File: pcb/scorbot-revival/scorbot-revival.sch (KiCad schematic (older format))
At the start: 4 parts, among them J1 DB-50, J2 Raspberry_Pi_2_3, U1 L293D, U2 PIC18F2431-E_SP

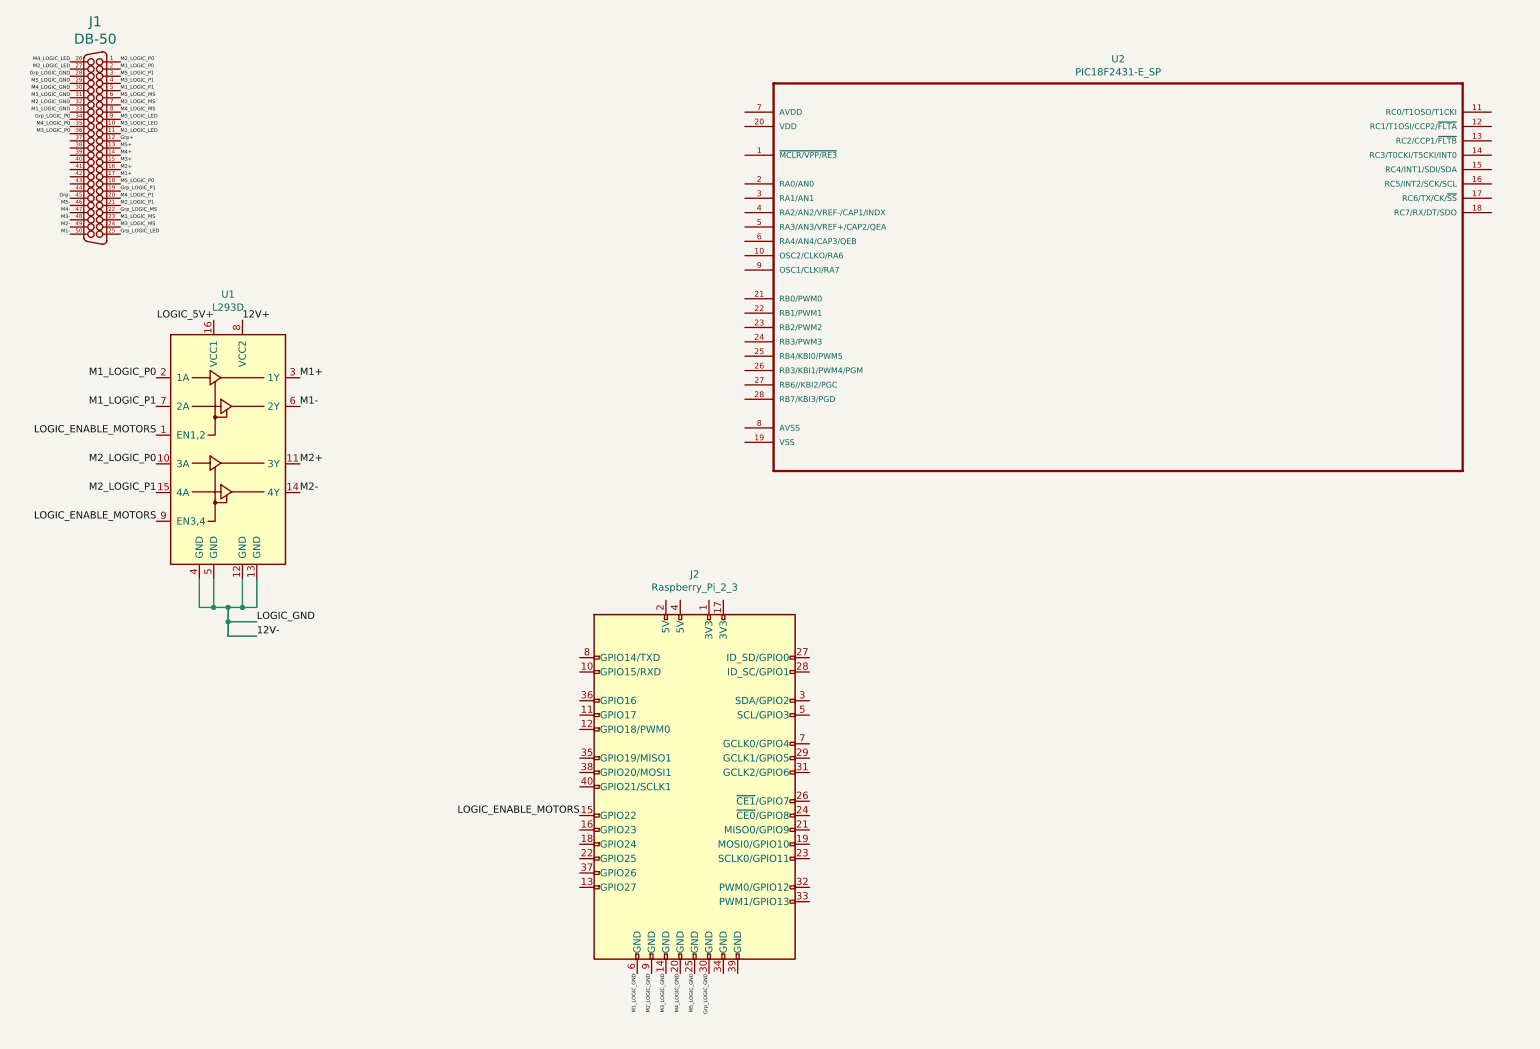
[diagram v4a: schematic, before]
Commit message: [pcb] pcbnew updates
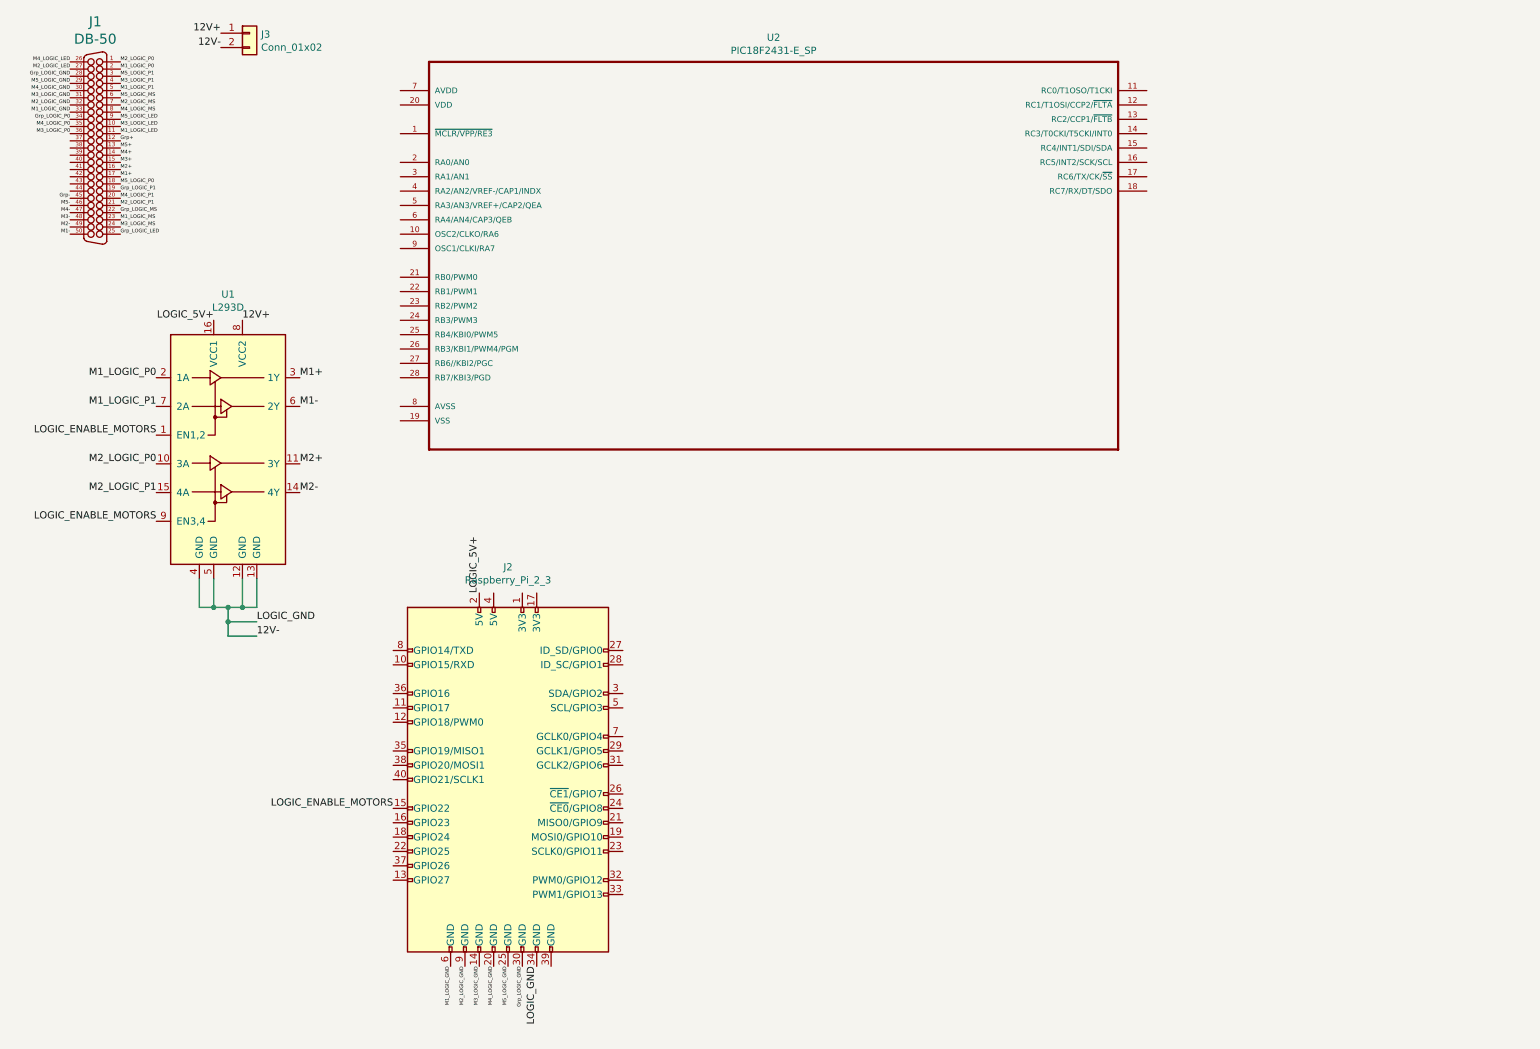
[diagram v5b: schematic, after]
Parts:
- added J3: Conn_01x02, Connector_BarrelJack:BarrelJack_Horizontal, symbol Connector_Generic:Conn_01x02
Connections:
- net 12V+: now also J3.1 (Pin_1)
- net 12V-: now also J2.34 (GND), J3.2 (Pin_2)
- net LOGIC_5V+: now also J2.2 (5V)
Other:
- moved on the sheet: J2, U2
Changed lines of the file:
@@
 Text Label 1250 1950 0    25   ~ 0
 Grp_LOGIC_MS
-Text Label 4850 7250 3    25   ~ 0
+Text Label 3550 7200 3    25   ~ 0
 M1_LOGIC_GND
-Text Label 4950 7250 3    25   ~ 0
+Text Label 3650 7200 3    25   ~ 0
 M2_LOGIC_GND
-Text Label 5050 7250 3    25   ~ 0
+Text Label 3750 7200 3    25   ~ 0
 M3_LOGIC_GND
-Text Label 5150 7250 3    25   ~ 0
+Text Label 3850 7200 3    25   ~ 0
 M4_LOGIC_GND
-Text Label 5250 7250 3    25   ~ 0
+Text Label 3950 7200 3    25   ~ 0
 M5_LOGIC_GND
-Text Label 5350 7250 3    25   ~ 0
+Text Label 4050 7200 3    25   ~ 0
 Grp_LOGIC_GND
 $Comp
 L PIC18F2431-E_SP:PIC18F2431-E_SP U2
 U 1 1 5E01D5FD
-P 8200 2250
-F 0 "U2" H 8200 3620 50  0000 C CNN
-F 1 "PIC18F2431-E_SP" H 8200 3529 50  0000 C CNN
-F 2 "Package_DIP:DIP-28_W7.62mm" H 8200 2250 50  0001 L BNN
-F 3 "PIC18F2431-E/SP-ND" H 8200 2250 50  0001 L BNN
-F 4 "SPDIP-28 Microchip" H 8200 2250 50  0001 L BNN "Field4"
-F 5 "PIC18F2431-E/SP" H 8200 2250 50  0001 L BNN "Field5"
-F 6 "https://www.digikey.com/product-detail/en/microchip-technology/PIC18F2431-E-SP/PIC18F2431-E-SP-ND/613546?utm_source=snapeda&utm_medium=aggregator&utm_campaign=symbol" H 8200 2250 50  0001 L BNN "Field6"
-F 7 "Microchip" H 8200 2250 50  0001 L BNN "Field7"
-F 8 "MCU 8-bit PIC18 PIC RISC 16KB Flash 5V 28-Pin SPDIP Tube" H 8200 2250 50  0001 L BNN "Field8"
-	1    8200 2250
+P 5800 2100
+F 0 "U2" H 5800 3470 50  0000 C CNN
+F 1 "PIC18F2431-E_SP" H 5800 3379 50  0000 C CNN
+F 2 "Package_DIP:DIP-28_W7.62mm" H 5800 2100 50  0001 L BNN
+F 3 "PIC18F2431-E/SP-ND" H 5800 2100 50  0001 L BNN
+F 4 "SPDIP-28 Microchip" H 5800 2100 50  0001 L BNN "Field4"
+F 5 "PIC18F2431-E/SP" H 5800 2100 50  0001 L BNN "Field5"
+F 6 "https://www.digikey.com/product-detail/en/microchip-technology/PIC18F2431-E-SP/PIC18F2431-E-SP-ND/613546?utm_source=snapeda&utm_medium=aggregator&utm_campaign=symbol" H 5800 2100 50  0001 L BNN "Field6"
+F 7 "Microchip" H 5800 2100 50  0001 L BNN "Field7"
+F 8 "MCU 8-bit PIC18 PIC RISC 16KB Flash 5V 28-Pin SPDIP Tube" H 5800 2100 50  0001 L BNN "Field8"
+	1    5800 2100
 	1    0    0    -1
 $EndComp
@@
 L Connector:Raspberry_Pi_2_3 J2
 U 1 1 5DE8F286
-P 5250 5950
-F 0 "J2" H 5250 7431 50  0000 C CNN
-F 1 "Raspberry_Pi_2_3" H 5250 7340 50  0000 C CNN
-F 2 "Connector_PinHeader_2.54mm:PinHeader_2x20_P2.54mm_Vertical" H 5250 5950 50  0001 C CNN
-F 3 "https://www.raspberrypi.org/documentation/hardware/raspberrypi/schematics/rpi_SCH_3bplus_1p0_reduced.pdf" H 5250 5950 50  0001 C CNN
-	1    5250 5950
+P 3950 5900
+F 0 "J2" H 3950 7381 50  0000 C CNN
+F 1 "Raspberry_Pi_2_3" H 3950 7290 50  0000 C CNN
+F 2 "Connector_PinHeader_2.54mm:PinHeader_2x20_P2.54mm_Vertical" H 3950 5900 50  0001 C CNN
+F 3 "https://www.raspberrypi.org/documentation/hardware/raspberrypi/schematics/rpi_SCH_3bplus_1p0_reduced.pdf" H 3950 5900 50  0001 C CNN
+	1    3950 5900
 	1    0    0    -1
 $EndComp
@@
 Text Label 1500 4100 2    50   ~ 0
 LOGIC_ENABLE_MOTORS
-Text Label 4450 6150 2    50   ~ 0
+Text Label 3150 6100 2    50   ~ 0
 LOGIC_ENABLE_MOTORS
+$Comp
+L Connector_Generic:Conn_01x02 J3
+U 1 1 5E136646
+P 2150 700
+F 0 "J3" H 2230 692 50  0000 L CNN
+F 1 "Conn_01x02" H 2230 601 50  0000 L CNN
+F 2 "Connector_BarrelJack:BarrelJack_Horizontal" H 2150 700 50  0001 C CNN
+F 3 "~" H 2150 700 50  0001 C CNN
+	1    2150 700
+	1    0    0    -1
+$EndComp
+Text Label 1950 700  2    50   ~ 0
+12V+
+Text Label 1950 800  2    50   ~ 0
+12V-
+Text Label 3750 4600 1    50   ~ 0
+LOGIC_5V+
+Text Label 4150 7200 3    50   ~ 0
+LOGIC_GND
 $EndSCHEMATC

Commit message: Added more L293Ds to net
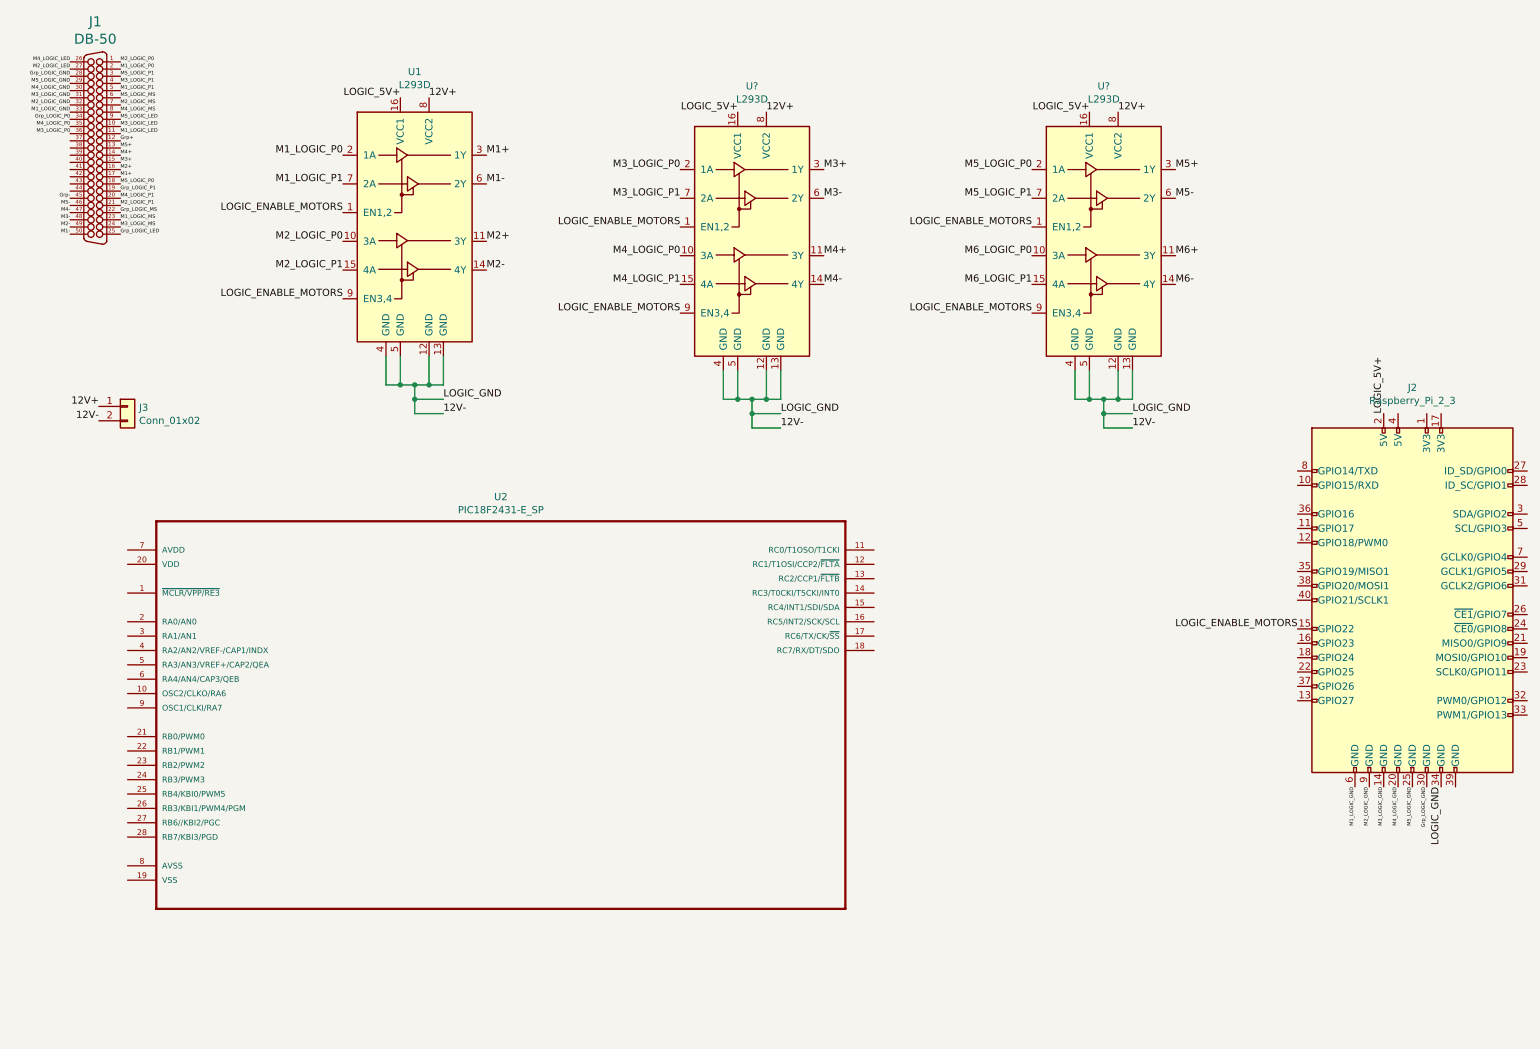
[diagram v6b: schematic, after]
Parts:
- added U? (x2): L293D, Package_DIP:DIP-16_W7.62mm, symbol Driver_Motor:L293D
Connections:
- net 12V+: now also U?.8 (VCC2), U?.8 (VCC2)
- net 12V-: now also U?.12 (GND), U?.12 (GND), U?.13 (GND), U?.13 (GND), U?.4 (GND), U?.4 (GND), U?.5 (GND), U?.5 (GND)
- net LOGIC_5V+: now also U?.16 (VCC1), U?.16 (VCC1)
- net LOGIC_ENABLE_MOTORS: now also U?.1 (EN1,2), U?.1 (EN1,2), U?.9 (EN3,4), U?.9 (EN3,4)
- net M3+: now also U?.3 (1Y)
- net M3-: now also U?.6 (2Y)
- net M3_LOGIC_P0: now also U?.2 (1A)
- net M3_LOGIC_P1: now also U?.7 (2A)
- net M4+: now also U?.11 (3Y)
- net M4-: now also U?.14 (4Y)
- net M4_LOGIC_P0: now also U?.10 (3A)
- net M4_LOGIC_P1: now also U?.15 (4A)
- net M5+: now also U?.3 (1Y)
- net M5-: now also U?.6 (2Y)
- net M5_LOGIC_P0: now also U?.2 (1A)
- net M5_LOGIC_P1: now also U?.7 (2A)
- new net M6+: U?.11 (3Y)
- new net M6-: U?.14 (4Y)
- new net M6_LOGIC_P0: U?.10 (3A)
- new net M6_LOGIC_P1: U?.15 (4A)
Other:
- moved on the sheet: J2, J3, U1, U2
